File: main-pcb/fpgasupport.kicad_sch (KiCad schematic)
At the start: 77 parts, among them J3 XILINX_JTAG, U1 XC7S100-1FGGA484C

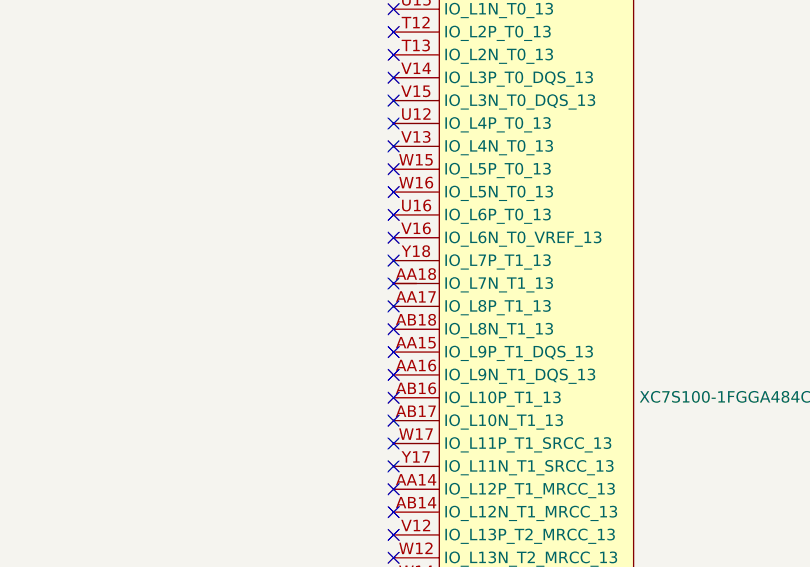
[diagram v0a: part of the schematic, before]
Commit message: Initial design mostly done aside from USB connector, review, test points
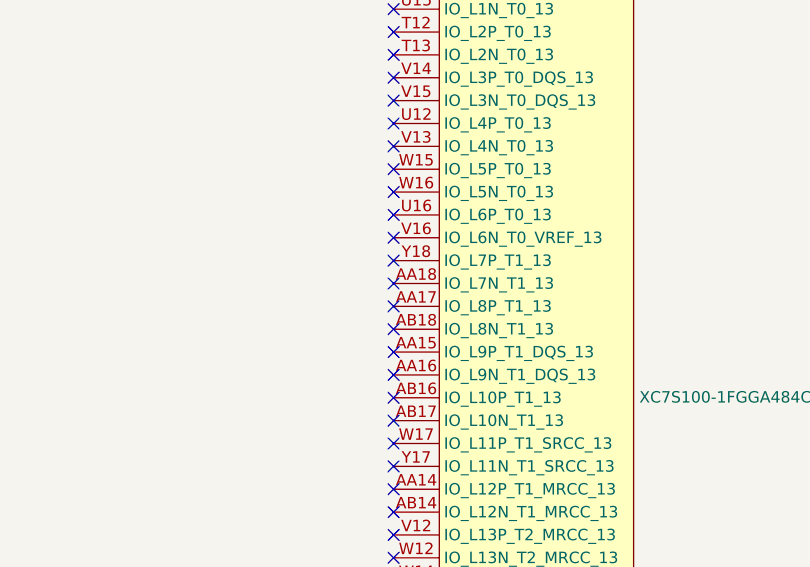
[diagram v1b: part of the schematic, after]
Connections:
- net at U1.AA18 (IO_L7N_T1_13): no longer U1.
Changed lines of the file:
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@@
 	(title_block
 		(title "DUMPTRUCK flash dumper")
-		(date "2024-10-14")
+		(date "2024-10-16")
 		(rev "0.1")
 		(company "Antikernel Labs")
@@
 	)
 	(no_connect
+		(at 224.79 58.42)
+	)
+	(no_connect
 		(at 224.79 116.84)
 	)
@@
 	)
 	(no_connect
-		(at 224.79 58.42)
-	)
-	(no_connect
 		(at 224.79 93.98)
 	)
@@
 		(pin "P9"
 		)
-		(pin ""
-		)
 		(pin "V12"
 		)
@@
 		(pin "P9"
 		)
-		(pin ""
-		)
 		(pin "V12"
 		)
@@
 		(pin "P9"
 		)
-		(pin ""
-		)
 		(pin "V12"
 		)
@@
 		(pin "P9"
 		)
-		(pin ""
-		)
 		(pin "V12"

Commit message: More schematic tweaks and test points
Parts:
- C17: footprint azonenberg_pcb:BGA_484_22x22_FULLARRAY_1MM -> (none)
- C18: footprint azonenberg_pcb:QFN_38_0.5MM_5x7MM -> (none)
- C20, C21, C22, C23, C24, C25, C36, C37, C38, C47, C48, C49, C50, C51, C52, C53, C54, C72, C73, C79, C80, C81, C82: footprint (none) -> azonenberg_pcb:EIA_0603_CAP_NOSILK
- C26, C27, C28, C29, C30, C31, C32, C33, C34, C39, C40, C41, C42, C43, C44, C45, C55, C56, C57, C58, C59, C60, C61, C62, C63, C64, C65, C66, C67, C68, C69, C70, C74, C75, C76, C77, C83, C84, C85, C86, C87, C88, C89, C90: footprint (none) -> azonenberg_pcb:EIA_0402_CAP_NOSILK
- R8: footprint (none) -> azonenberg_pcb:EIA_0402_RES_NOSILK

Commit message: Added some RGB LEDs, changed a few voltage dividers to match what was in stock. Time for next round of review.
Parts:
- C17, C18, C46: footprint (none) -> azonenberg_pcb:EIA_1206_CAP_NOSILK
- C19, C35, C71, C78: footprint (none) -> azonenberg_pcb:EIA_1210_CAP_NOSILK
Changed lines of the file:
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@@
 	(title_block
 		(title "DUMPTRUCK flash dumper")
-		(date "2024-10-16")
+		(date "2024-10-17")
 		(rev "0.1")
 		(company "Antikernel Labs")
@@
 			)
 		)
-		(property "Footprint" ""
+		(property "Footprint" "azonenberg_pcb:EIA_1206_CAP_NOSILK"
 			(at 138.1252 161.29 0)
 			(effects
@@
 			)
 		)
-		(property "Footprint" ""
+		(property "Footprint" "azonenberg_pcb:EIA_1210_CAP_NOSILK"
 			(at 124.1552 190.5 0)
 			(effects
@@
 			)
 		)
-		(property "Footprint" ""
+		(property "Footprint" "azonenberg_pcb:EIA_1206_CAP_NOSILK"
 			(at 124.1552 214.63 0)
 			(effects
@@
 			)
 		)
-		(property "Footprint" ""
+		(property "Footprint" "azonenberg_pcb:EIA_1210_CAP_NOSILK"
 			(at 124.1552 248.92 0)
 			(effects
@@
 			)
 		)
-		(property "Footprint" ""
+		(property "Footprint" "azonenberg_pcb:EIA_1210_CAP_NOSILK"
 			(at 124.1552 262.89 0)
 			(effects
@@
 			)
 		)
-		(property "Footprint" ""
+		(property "Footprint" "azonenberg_pcb:EIA_1206_CAP_NOSILK"
 			(at 124.1552 161.29 0)
 			(effects
@@
 			)
 		)
-		(property "Footprint" ""
+		(property "Footprint" "azonenberg_pcb:EIA_1210_CAP_NOSILK"
 			(at 150.8252 161.29 0)
 			(effects

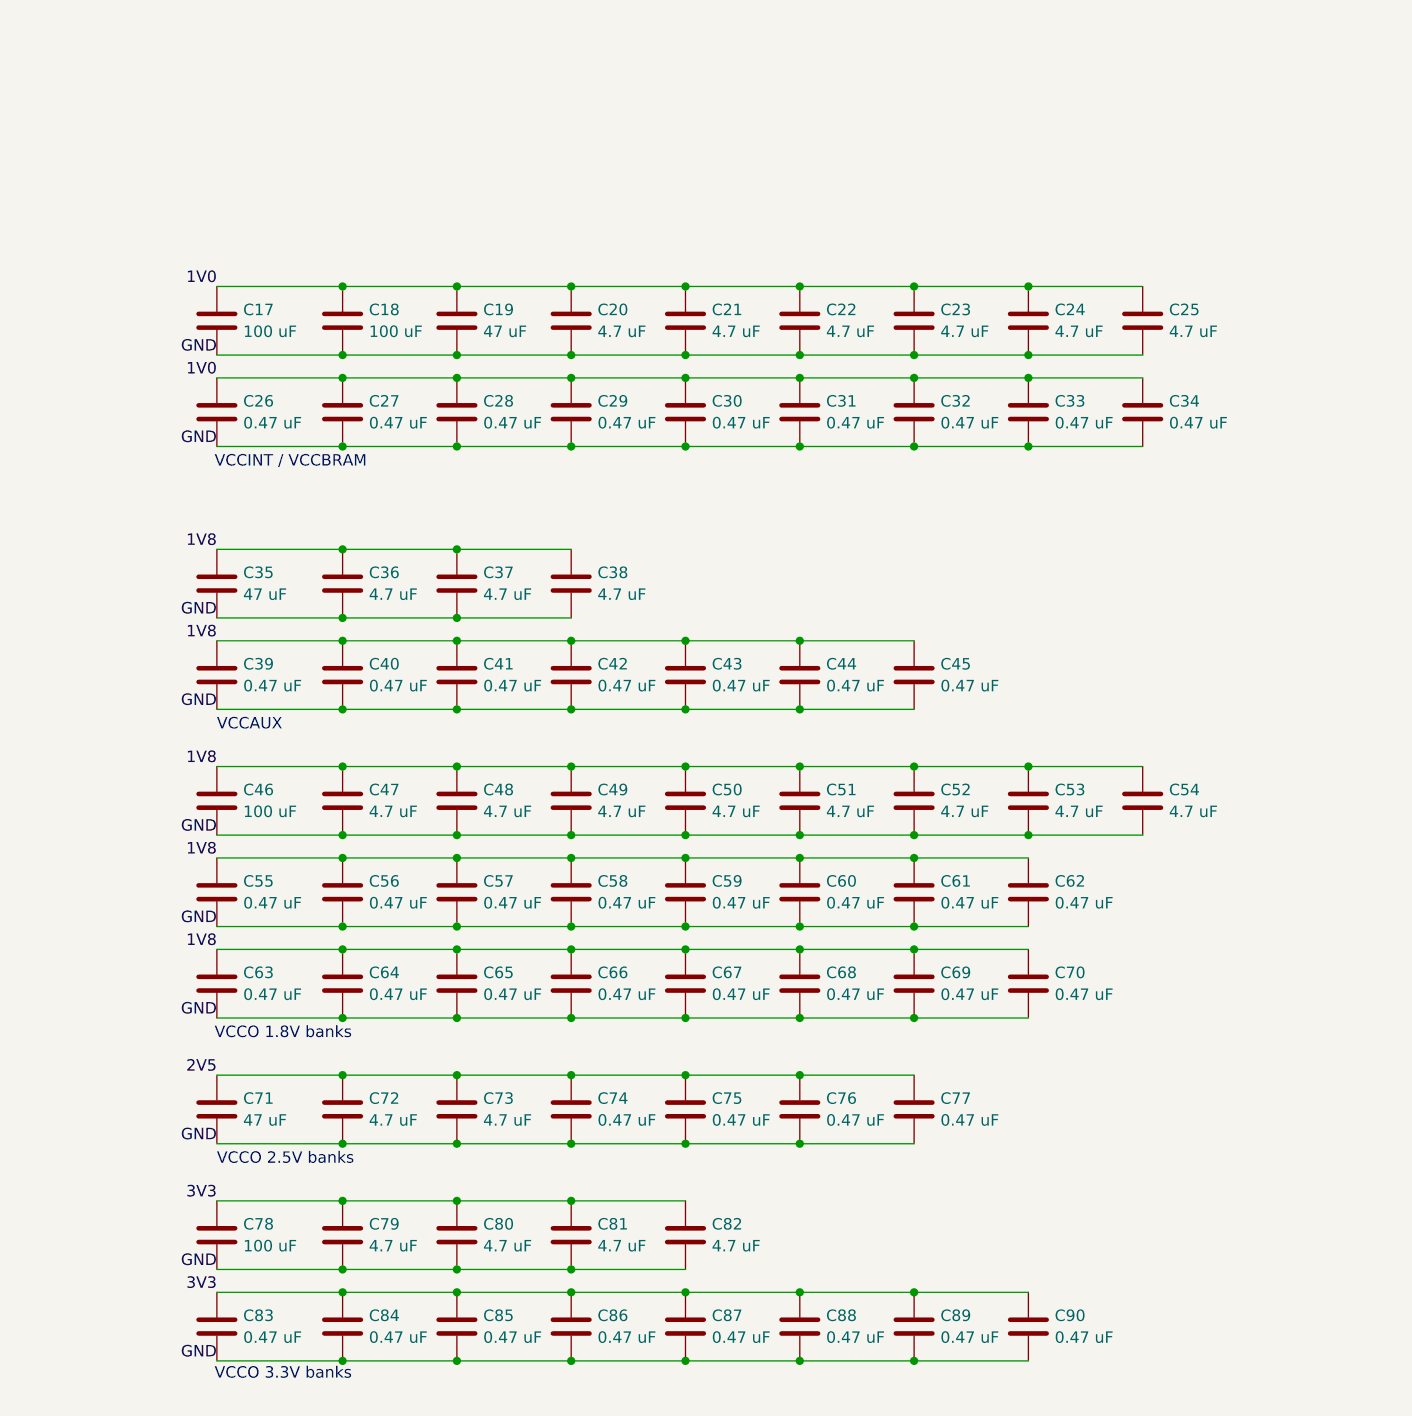
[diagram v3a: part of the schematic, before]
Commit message: First DUT socket fully routed
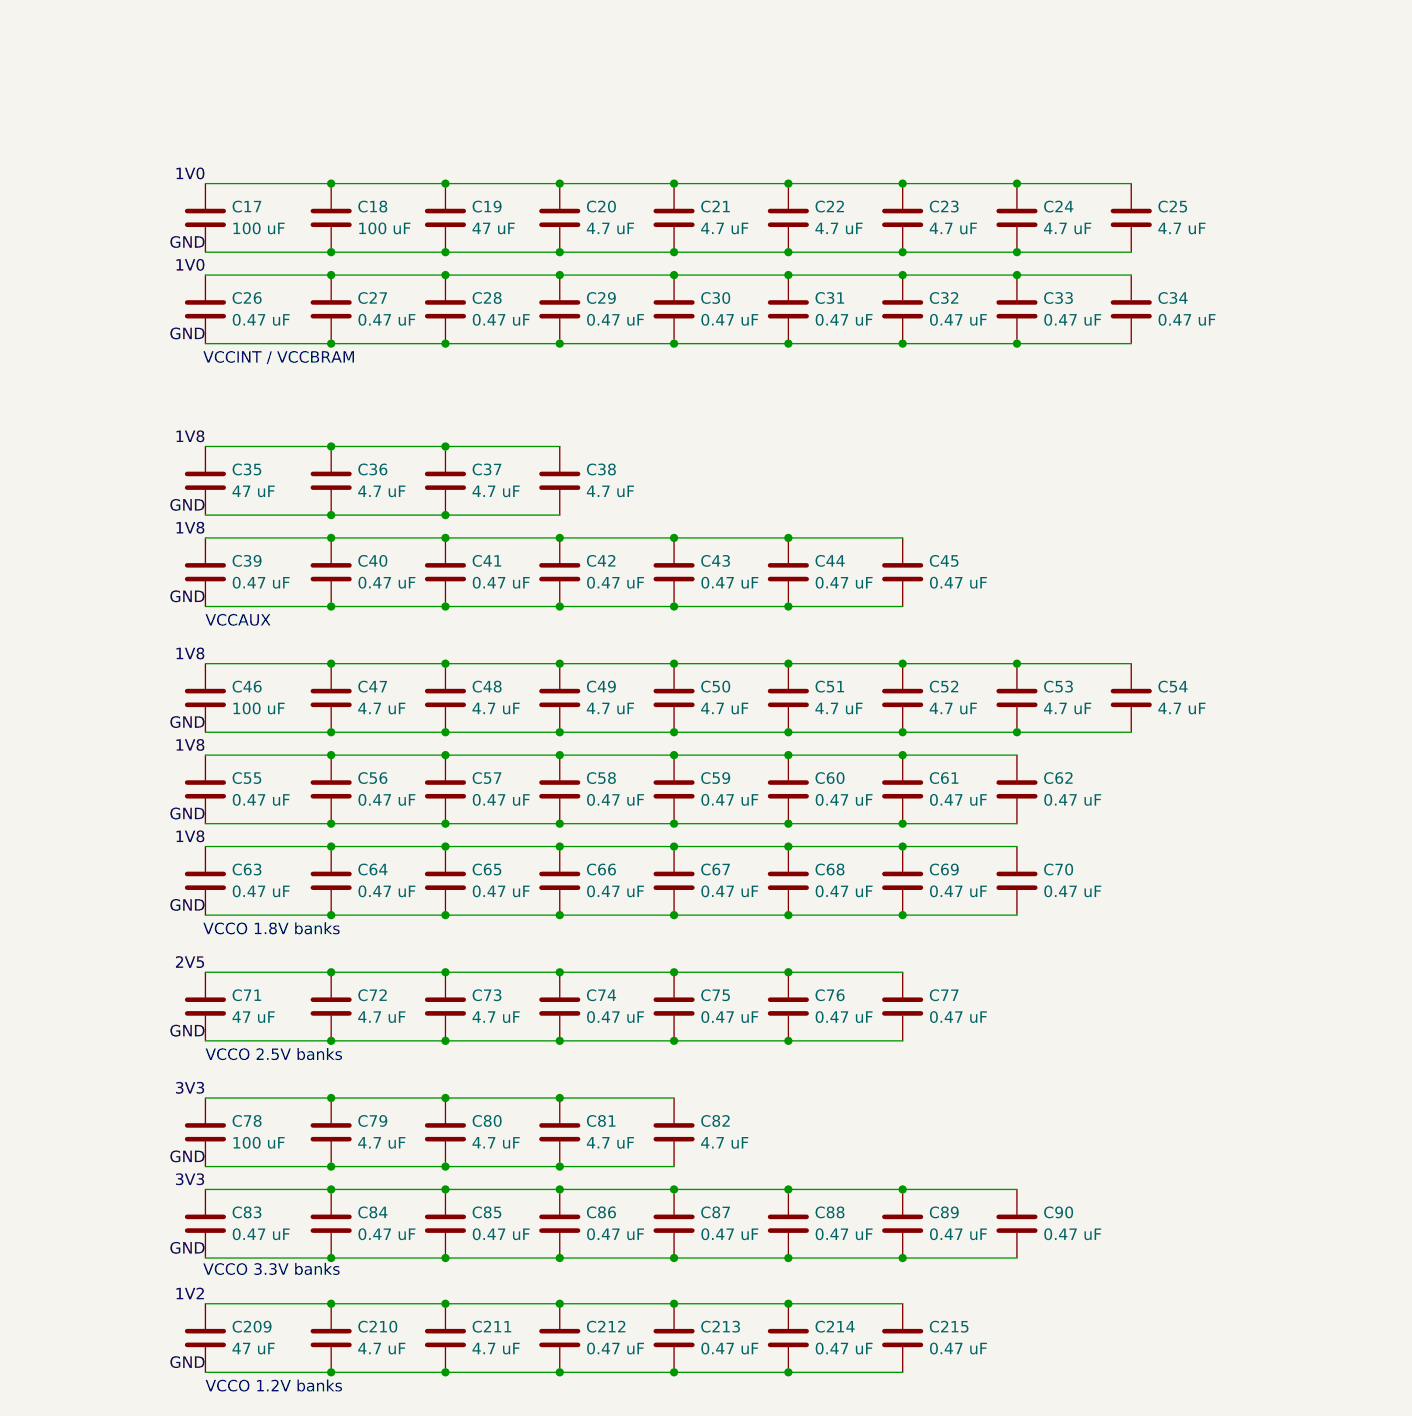
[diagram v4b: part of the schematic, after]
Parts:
- added C209: 47 uF, azonenberg_pcb:EIA_1210_CAP_NOSILK, symbol device:C
- added C210, C211: 4.7 uF, azonenberg_pcb:EIA_0603_CAP_NOSILK, symbol device:C
- added C212, C213, C214, C215: 0.47 uF, azonenberg_pcb:EIA_0402_CAP_NOSILK, symbol device:C
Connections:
- net 1V2: now also C209.1, C210.1, C211.1, C212.1, C213.1, C214.1, C215.1
- net GND: now also C209.2, C210.2, C211.2, C212.2, C213.2, C214.2, C215.2
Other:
- note added: "VCCO 1.2V banks"
- moved on the sheet: C17, C18, C19, C20, C21, C22, C23, C24, C25, C26, C27, C28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

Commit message: Continued routing MCU, started work on PHY
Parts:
- added R110: 33, azonenberg_pcb:EIA_0402_RES_NOSILK, symbol device:R
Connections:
- net FPGA_FLASH_SCK: now also R110.2; no longer U1.D9 (CCLK_0)
- new net: R110.1, U1.D9 (CCLK_0)
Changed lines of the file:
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@@
 	(title_block
 		(title "DUMPTRUCK flash dumper")
-		(date "2024-10-19")
+		(date "2024-10-20")
 		(rev "0.1")
 		(company "Antikernel Labs")
@@
 	(wire
 		(pts
+			(xy 165.1 22.86) (xy 167.64 22.86)
+		)
+		(stroke
+			(width 0)
+			(type default)
+		)
+	)
+	(wire
+		(pts
 			(xy 30.48 68.58) (xy 30.48 71.12)
 		)
@@
 	(wire
 		(pts
+			(xy 175.26 22.86) (xy 185.42 22.86)
+		)
+		(stroke
+			(width 0)
+			(type default)
+		)
+	)
+	(wire
+		(pts
 			(xy 199.39 142.24) (xy 212.09 142.24)
 		)
@@
 	(hierarchical_label "FPGA_FLASH_SCK"
 		(shape output)
-		(at 165.1 22.86 0)
+		(at 185.42 22.86 0)
 		(fields_autoplaced yes)
 		(effects
@@
 					(unit 1)
 				)
+			)
+		)
+	)
+	(symbol
+		(lib_id "device:R")
+		(at 171.45 22.86 90)
+		(unit 1)
+		(exclude_from_sim no)
+		(in_bom yes)
+		(on_board yes)
+		(dnp no)
+		(property "Reference" "R110"
+			(at 175.26 21.59 90)
+			(effects
+				(font
+					(size 1.27 1.27)
+				)
+			)
+		)
+		(property "Value" "33"
+			(at 171.45 22.86 90)
+			(effects
+				(font
+					(size 1.27 1.27)
+				)
+			)
+		)
+		(property "Footprint" "azonenberg_pcb:EIA_0402_RES_NOSILK"
+			(at 171.45 24.638 90)
+			(effects
+				(font
+					(size 1.27 1.27)
+				)
+				(hide yes)
+			)
+		)
+		(property "Datasheet" ""
+			(at 171.45 22.86 0)
+			(effects
+				(font
+					(size 1.27 1.27)
+				)
+				(hide yes)
+			)
+		)
+		(property "Description" ""
+			(at 171.45 22.86 0)
+			(effects
+				(font
+					(size 1.27 1.27)
+				)
+				(hide yes)
+			)
+		)
+		(pin "1"
+		)
+		(pin "2"
+		)
+		(instances
+			(project "main-pcb"
+				(path "/e33e9f2b-a48c-455d-96ec-c7304b1720d3/7cd2e806-1202-4934-b0af-c6f98384d647"
+					(reference "R110")
+					(unit 1)
+				)
